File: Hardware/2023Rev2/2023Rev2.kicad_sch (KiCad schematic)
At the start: 93 parts, among them J2 Conn_01x03, J3 Conn_01x03, J4 Conn_01x02, J5 Conn_01x09, J6 Conn_01x09, J7 RJ45_LED_Shielded, J9 Conn_01x04, Q2 Q_NMOS_DGS, Q3 Q_NMOS_DGS, Q4 Q_NMOS_DGS, Q5 Q_NMOS_GDS, U10 LT1910, U11 TSR_1-2450, U2 Opamp_Dual, U3 Teensy4.1_DEV-16771, U4 Opamp_Dual, U5 Opamp_Dual, U6 Opamp_Dual, U7 ACS758xCB-200B-PFF, U8 BMS_Logic_Switch, U9 OKI

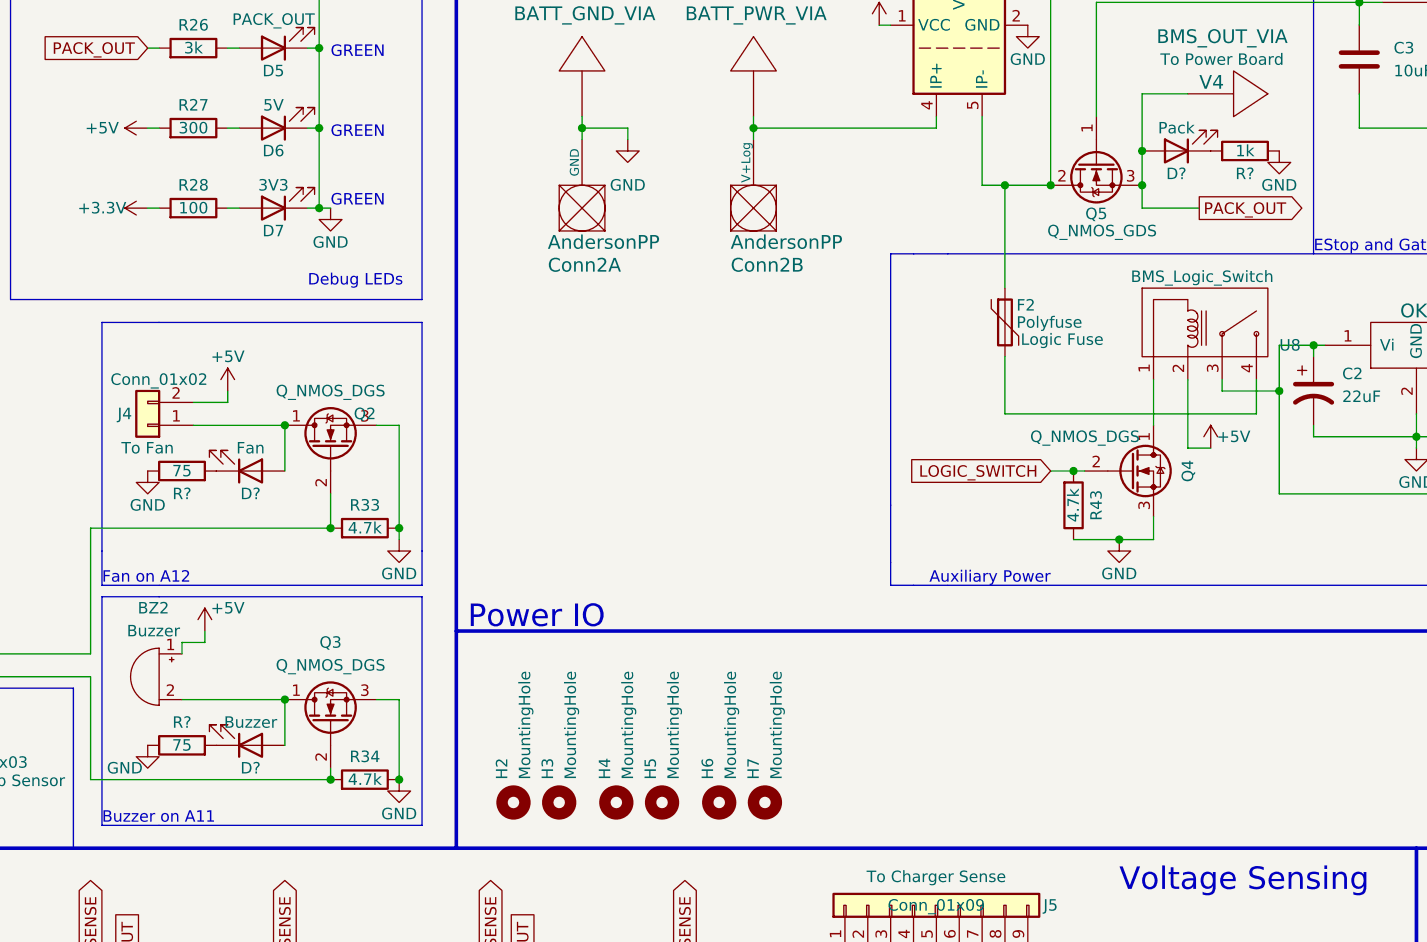
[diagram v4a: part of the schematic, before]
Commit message: fixed nfet layout
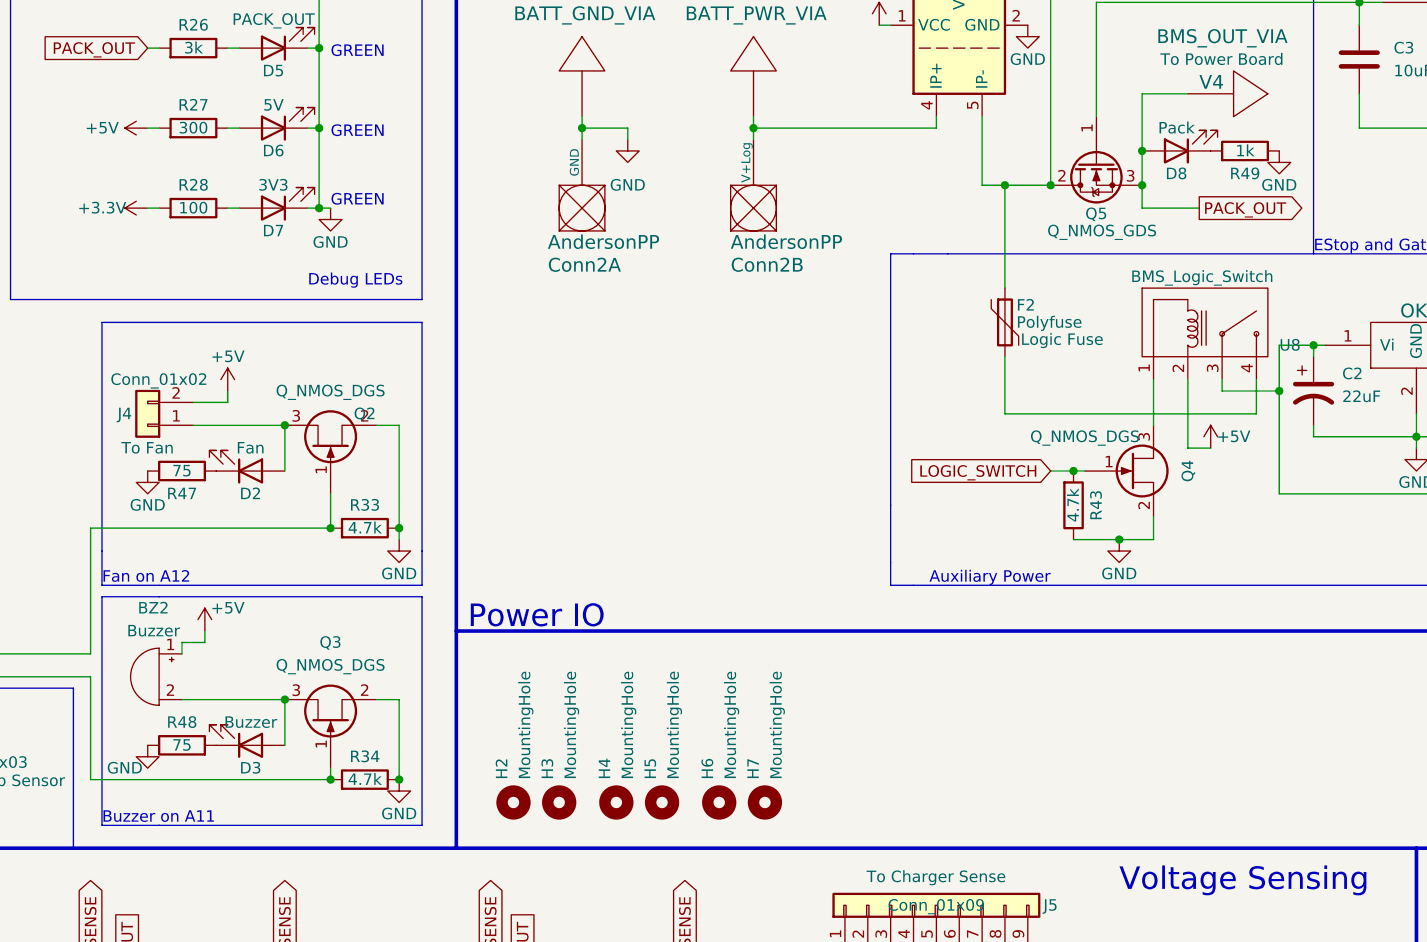
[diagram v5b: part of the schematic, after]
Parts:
- Q2, Q3, Q4: symbol Device:Q_NMOS_DGS -> Device:Q_NJFET_GSD
- gave numbers to parts that had none: 6
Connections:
- net GND: now also Q2.2 (S), Q3.2 (S), Q4.2 (S); no longer Q2.3 (S), Q3.3 (S), Q4.3 (S)
- net LOGIC_SWITCH: now also Q4.1 (G); no longer Q4.2 (G)
- net at D2.2 (A), J4.1 (Pin_1): now also Q2.3 (D); no longer Q2.1 (D)
- net at R33.2, U3.26 (A12): now also Q2.1 (G); no longer Q2.2 (G)
- net at U8.1: now also Q4.3 (D); no longer Q4.1 (D)
- net at BZ2.2 (+), D3.2 (A): now also Q3.3 (D); no longer Q3.1 (D)
- net at R34.2, U3.25 (A11): now also Q3.1 (G); no longer Q3.2 (G)
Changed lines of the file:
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@@
   (symbol (lib_id "power:GND") (at 251.46 41.91 0) (mirror y) (unit 1)
     (in_bom yes) (on_board yes)
-    (property "Reference" "#PWR?" (id 0) (at 251.46 48.26 0)
+    (property "Reference" "#PWR0103" (id 0) (at 251.46 48.26 0)
       (effects (font (size 1.27 1.27)) hide)
     )
@@
     (pin "1")
   )
-  (symbol (lib_id "Device:Q_NMOS_DGS") (at 146.05 74.93 90) (unit 1)
+  (symbol (lib_id "Device:Q_NJFET_GSD") (at 146.05 74.93 90) (unit 1)
     (in_bom yes) (on_board yes)
     (property "Reference" "Q2" (id 0) (at 149.86 71.12 90))
@@
   (symbol (lib_id "Device:R") (at 129.54 107.95 90) (unit 1)
     (in_bom yes) (on_board yes)
-    (property "Reference" "R?" (id 0) (at 129.54 105.41 90))
+    (property "Reference" "R48" (id 0) (at 129.54 105.41 90))
     (property "Value" "75" (id 1) (at 129.54 107.95 90))
     (property "Footprint" "" (id 2) (at 129.54 109.728 90)
@@
     (pin "2")
   )
-  (symbol (lib_id "Device:Q_NMOS_DGS") (at 234.95 77.47 0) (unit 1)
+  (symbol (lib_id "Device:Q_NJFET_GSD") (at 234.95 77.47 0) (unit 1)
     (in_bom yes) (on_board yes)
     (property "Reference" "Q4" (id 0) (at 241.3 77.47 90))
@@
   (symbol (lib_id "Device:LED") (at 240.03 41.91 180) (unit 1)
     (in_bom yes) (on_board yes)
-    (property "Reference" "D?" (id 0) (at 240.03 44.45 0))
+    (property "Reference" "D8" (id 0) (at 240.03 44.45 0))
     (property "Value" "Pack" (id 1) (at 240.03 39.37 0))
     (property "Footprint" "LED_SMD:LED_0603_1608Metric_Pad1.05x0.95mm_HandSolder" (id 2) (at 240.03 41.91 0)
@@
   (symbol (lib_id "Device:LED") (at 137.16 107.95 0) (mirror x) (unit 1)
     (in_bom yes) (on_board yes)
-    (property "Reference" "D?" (id 0) (at 137.16 110.49 0))
+    (property "Reference" "D3" (id 0) (at 137.16 110.49 0))
     (property "Value" "Buzzer" (id 1) (at 137.16 105.41 0))
     (property "Footprint" "LED_SMD:LED_0603_1608Metric_Pad1.05x0.95mm_HandSolder" (id 2) (at 137.16 107.95 0)
@@
   (symbol (lib_id "Device:R") (at 247.65 41.91 270) (mirror x) (unit 1)
     (in_bom yes) (on_board yes)
-    (property "Reference" "R?" (id 0) (at 247.65 44.45 90))
+    (property "Reference" "R49" (id 0) (at 247.65 44.45 90))
     (property "Value" "1k" (id 1) (at 247.65 41.91 90))
     (property "Footprint" "" (id 2) (at 247.65 43.688 90)
@@
   (symbol (lib_id "power:GND") (at 125.73 77.47 0) (unit 1)
     (in_bom yes) (on_board yes)
-    (property "Reference" "#PWR?" (id 0) (at 125.73 83.82 0)
+    (property "Reference" "#PWR0104" (id 0) (at 125.73 83.82 0)
       (effects (font (size 1.27 1.27)) hide)
     )
@@
   (symbol (lib_id "Device:R") (at 129.54 77.47 90) (unit 1)
     (in_bom yes) (on_board yes)
-    (property "Reference" "R?" (id 0) (at 129.54 80.01 90))
+    (property "Reference" "R47" (id 0) (at 129.54 80.01 90))
     (property "Value" "75" (id 1) (at 129.54 77.47 90))
     (property "Footprint" "" (id 2) (at 129.54 79.248 90)
@@
     (pin "2")
   )
-  (symbol (lib_id "Device:Q_NMOS_DGS") (at 146.05 105.41 90) (unit 1)
+  (symbol (lib_id "Device:Q_NJFET_GSD") (at 146.05 105.41 90) (unit 1)
     (in_bom yes) (on_board yes)
     (property "Reference" "Q3" (id 0) (at 146.05 96.52 90))
@@
   (symbol (lib_id "Device:LED") (at 137.16 77.47 0) (mirror x) (unit 1)
     (in_bom yes) (on_board yes)
-    (property "Reference" "D?" (id 0) (at 137.16 80.01 0))
+    (property "Reference" "D2" (id 0) (at 137.16 80.01 0))
     (property "Value" "Fan" (id 1) (at 137.16 74.93 0))
     (property "Footprint" "LED_SMD:LED_0603_1608Metric_Pad1.05x0.95mm_HandSolder" (id 2) (at 137.16 77.47 0)
@@
     )
     (path "/033cb383-27fd-45cb-b366-0d48e4205c32"
-      (reference "#PWR?") (unit 1) (value "GND") (footprint "")
+      (reference "#PWR0103") (unit 1) (value "GND") (footprint "")
     )
     (path "/d7930b83-8ee7-49c0-8025-db61211de7af"
-      (reference "#PWR?") (unit 1) (value "GND") (footprint "")
+      (reference "#PWR0104") (unit 1) (value "GND") (footprint "")
     )
     (path "/c98bd7a4-fa5b-4a36-a243-d06d89cb06bb"
@@
       (reference "Conn2") (unit 2) (value "AndersonPP") (footprint "MRDT_Connectors:Square_Anderson_2_V_Side_By_Side")
     )
+    (path "/fbe93978-0994-48b6-bbdb-e5536ad91212"
+      (reference "D2") (unit 1) (value "Fan") (footprint "LED_SMD:LED_0603_1608Metric_Pad1.05x0.95mm_HandSolder")
+    )
+    (path "/aef649cf-d67b-4e0d-9ceb-2f2c8269e75a"
+      (reference "D3") (unit 1) (value "Buzzer") (footprint "LED_SMD:LED_0603_1608Metric_Pad1.05x0.95mm_HandSolder")
+    )
     (path "/81187ef8-a89f-4382-a9cd-107587c14c9d"
       (reference "D4") (unit 1) (value "ERR") (footprint "LED_SMD:LED_0603_1608Metric_Pad1.05x0.95mm_HandSolder")
@@
     )
     (path "/797531bd-dd3e-4633-83df-6d2246baac9c"
-      (reference "D?") (unit 1) (value "Pack") (footprint "LED_SMD:LED_0603_1608Metric_Pad1.05x0.95mm_HandSolder")
-    )
-    (path "/aef649cf-d67b-4e0d-9ceb-2f2c8269e75a"
-      (reference "D?") (unit 1) (value "Buzzer") (footprint "LED_SMD:LED_0603_1608Metric_Pad1.05x0.95mm_HandSolder")
-    )
-    (path "/fbe93978-0994-48b6-bbdb-e5536ad91212"
-      (reference "D?") (unit 1) (value "Fan") (footprint "LED_SMD:LED_0603_1608Metric_Pad1.05x0.95mm_HandSolder")
+      (reference "D8") (unit 1) (value "Pack") (footprint "LED_SMD:LED_0603_1608Metric_Pad1.05x0.95mm_HandSolder")
     )
     (path "/4a07cea7-5747-4143-a41e-1a5f0c72b583"
@@
       (reference "R46") (unit 1) (value "10k") (footprint "Resistor_SMD:R_0603_1608Metric_Pad0.98x0.95mm_HandSolder")
     )
+    (path "/d7c5f1ba-edc4-4871-a4c2-51b3dcec946d"
+      (reference "R47") (unit 1) (value "75") (footprint "")
+    )
     (path "/1a597589-acb4-455b-9ad7-a3d40996a755"
-      (reference "R?") (unit 1) (value "75") (footprint "")
+      (reference "R48") (unit 1) (value "75") (footprint "")
     )
     (path "/bc97fd74-eddc-4a06-9450-55bf7a4c21f7"
-      (reference "R?") (unit 1) (value "1k") (footprint "")
-    )
-    (path "/d7c5f1ba-edc4-4871-a4c2-51b3dcec946d"
-      (reference "R?") (unit 1) (value "75") (footprint "")
+      (reference "R49") (unit 1) (value "1k") (footprint "")
     )
     (path "/73bcadae-54dc-43c9-91fa-c33fb02a16fb"

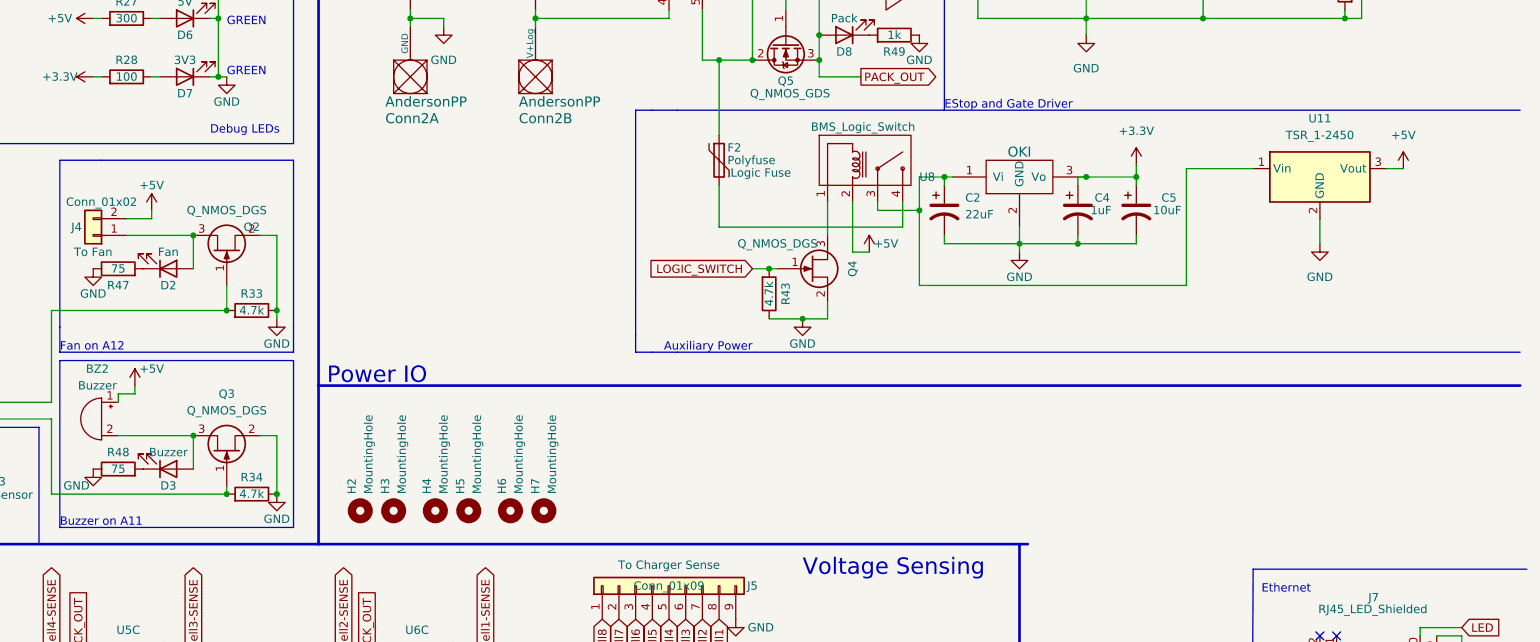
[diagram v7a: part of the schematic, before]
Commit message: added caps to tsr and leds to mosfets
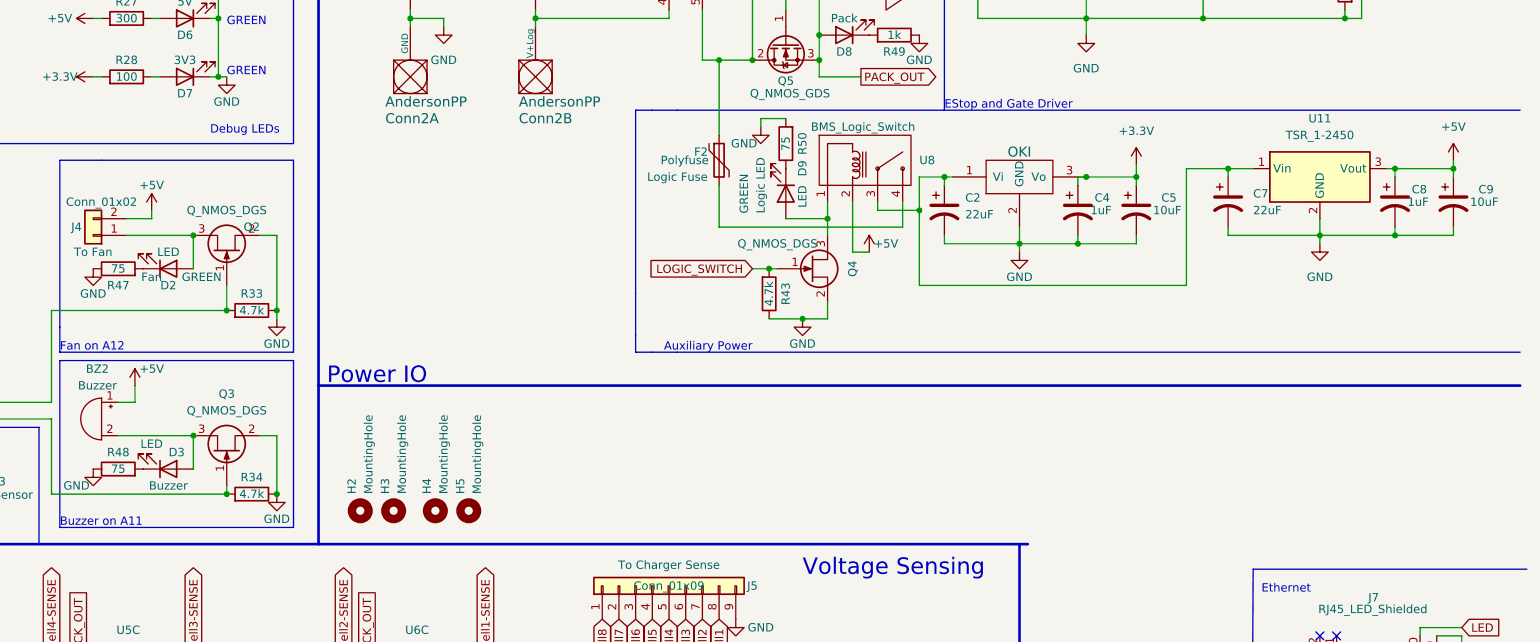
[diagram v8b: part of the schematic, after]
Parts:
- removed H6, H7: MountingHole, MRDT_Drill_Holes:4_40_Hole, symbol Mechanical:MountingHole
- added C7: 22uF, Capacitor_SMD:C_0603_1608Metric_Pad1.08x0.95mm_HandSolder, symbol Device:C_Polarized_US
- added C8: 1uF, Capacitor_SMD:C_0603_1608Metric_Pad1.08x0.95mm_HandSolder, symbol Device:C_Polarized_US
- added C9: 10uF, Capacitor_SMD:C_0603_1608Metric_Pad1.08x0.95mm_HandSolder, symbol Device:C_Polarized_US
- added D9: LED, LED_SMD:LED_0603_1608Metric_Pad1.05x0.95mm_HandSolder, symbol Device:LED
- added R50: 75, Resistor_SMD:R_0603_1608Metric_Pad0.98x0.95mm_HandSolder, symbol Device:R
- D2: value Fan -> LED; Field4 (none) -> Fan; Field5 (none) -> GREEN
- D3: value Buzzer -> LED; Field4 (none) -> Buzzer
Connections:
- net +5V: now also C8.1, C9.1
- net GND: now also C7.2, C8.2, C9.2, R50.2
- net at Q4.3 (D), U8.1: now also D9.2 (A)
- net at C2.1, U11.1 (Vin), U8.3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: now also C7.1
- new net: D9.1 (K), R50.1
